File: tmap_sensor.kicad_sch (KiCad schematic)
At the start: 6 parts, among them J18 Conn_01x90_3Row_Socket, K2 1500A, K3 1502, K4 1500B, M2 Fan1, M3 Fan2

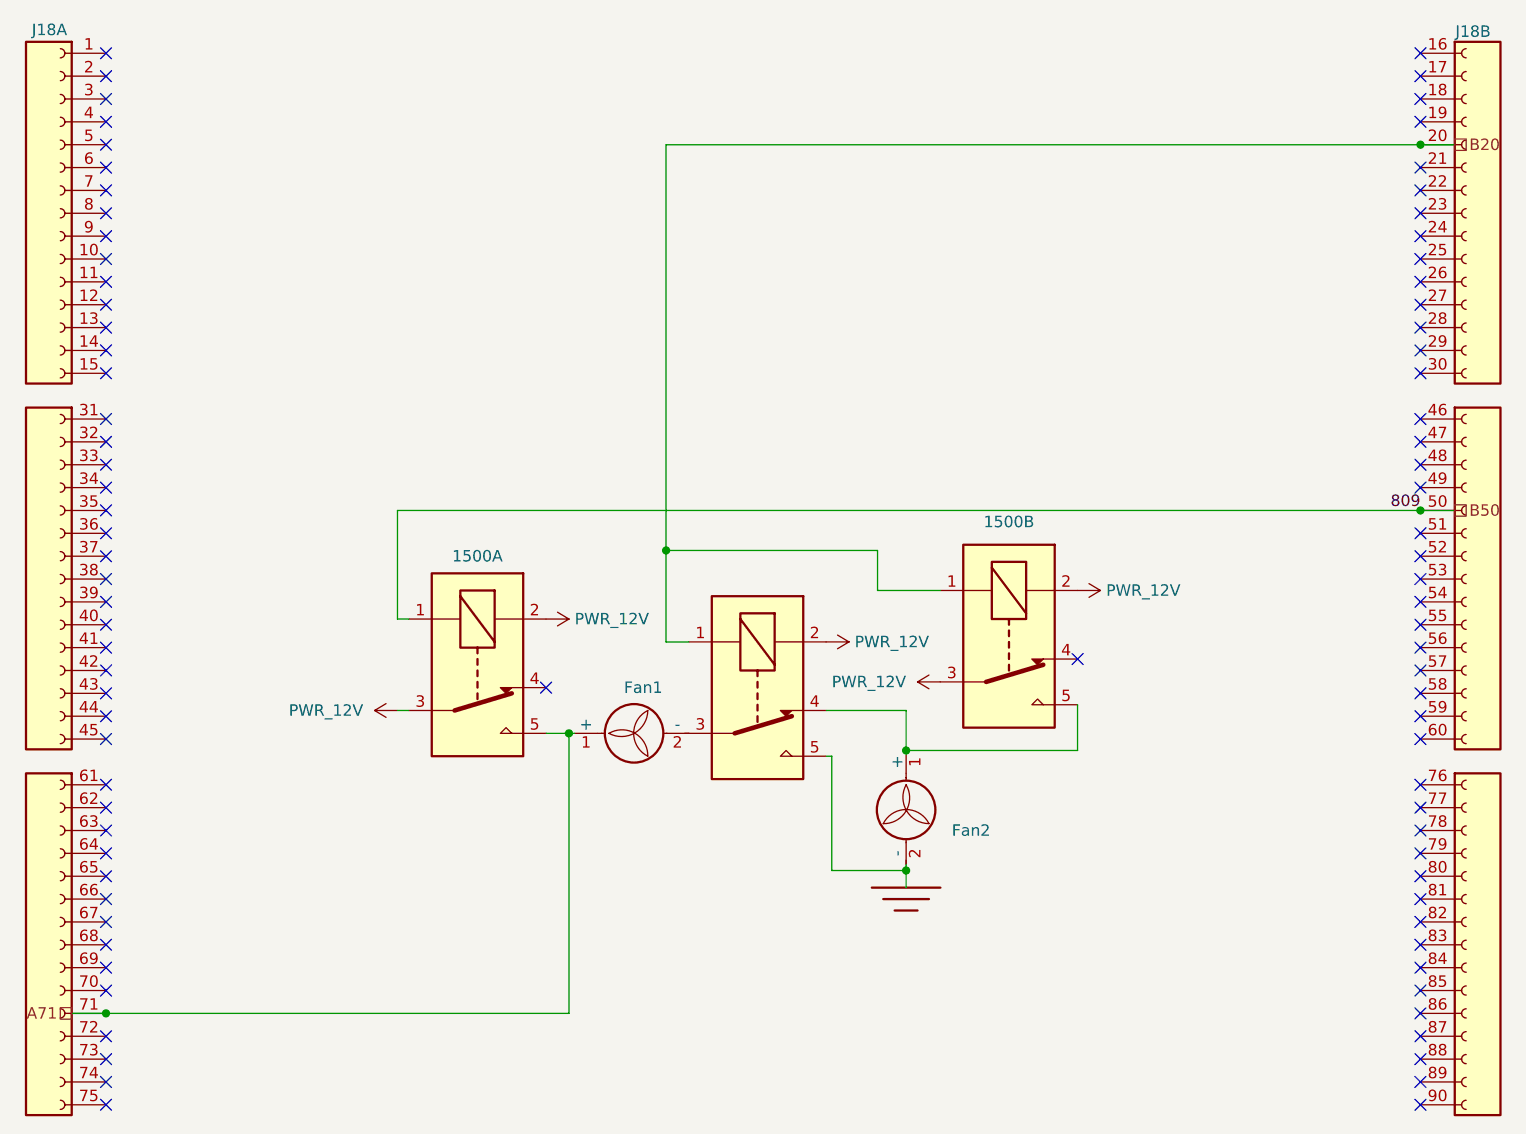
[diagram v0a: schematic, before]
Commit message: air conditioner updated
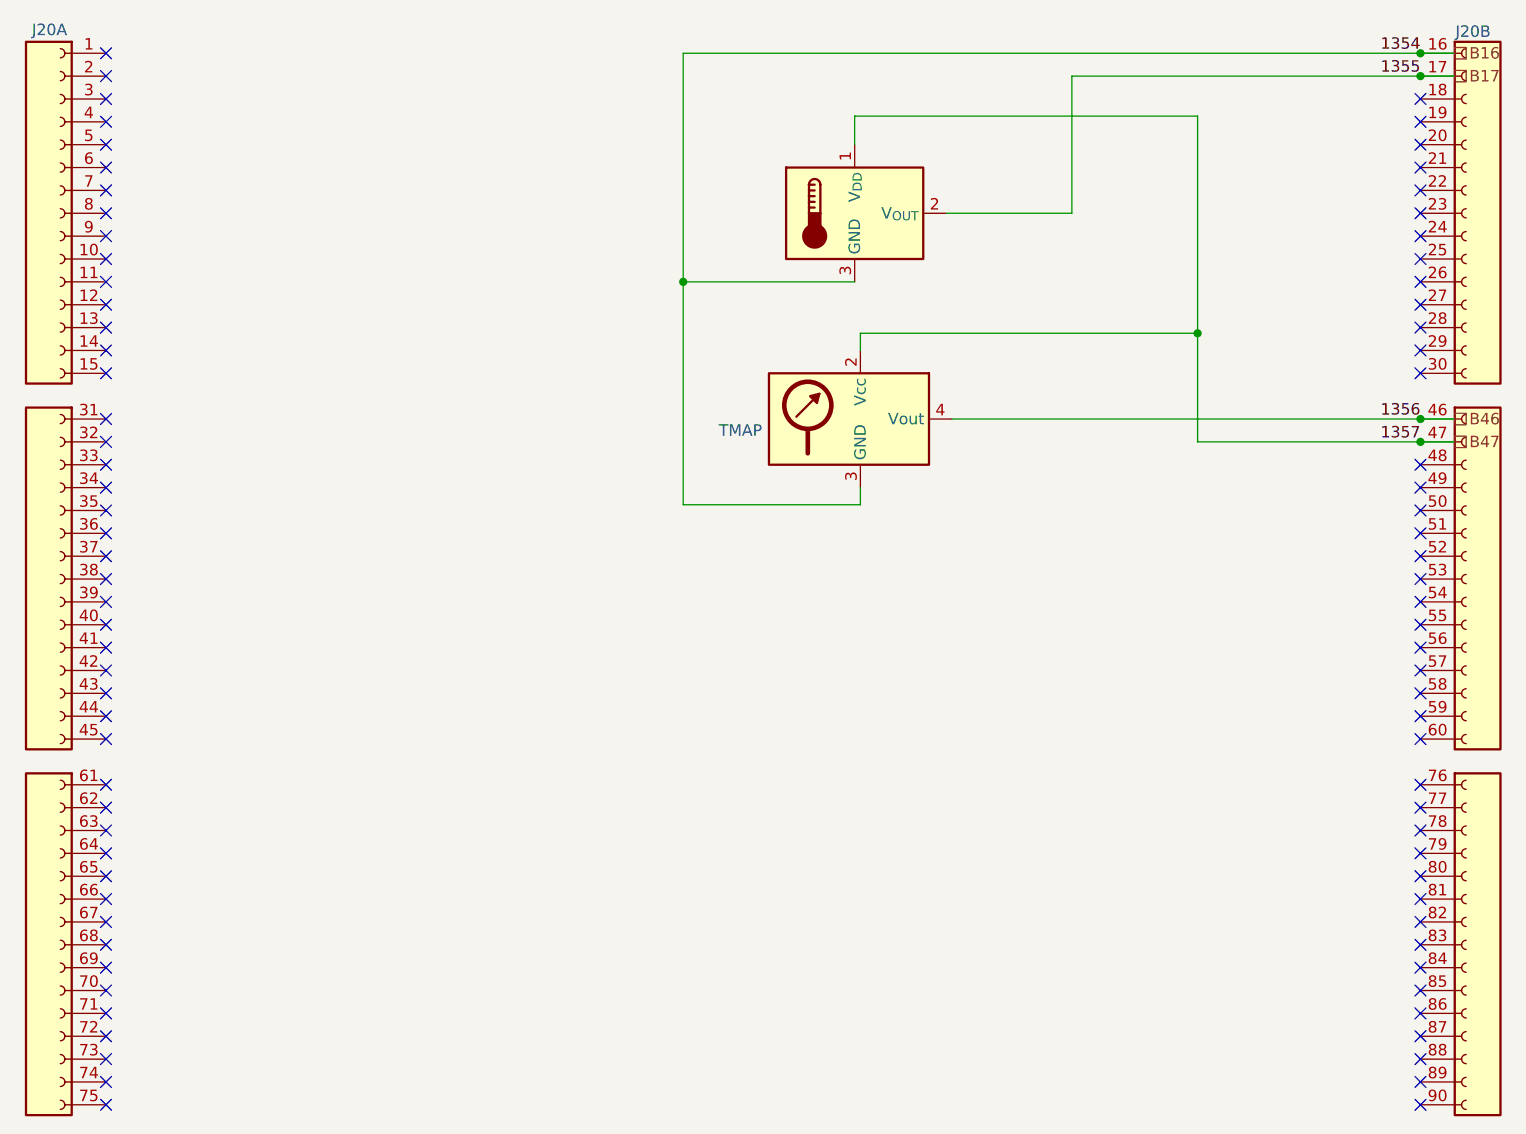
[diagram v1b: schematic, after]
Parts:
- removed J18: Conn_01x90_3Row_Socket, symbol sicma_socket:Conn_01x90_3Row_Socket
- removed K2: 1500A, PCM_SparkFun-Electromechanical:Relay_SPDT_20A_27.6x32.0mm, symbol SparkFun-Electromechanical:Relay_SPDT_20A_5V_27.6x32.0mm
- removed K3: 1502, PCM_SparkFun-Electromechanical:Relay_SPDT_20A_27.6x32.0mm, symbol SparkFun-Electromechanical:Relay_SPDT_20A_5V_27.6x32.0mm
- removed K4: 1500B, PCM_SparkFun-Electromechanical:Relay_SPDT_20A_27.6x32.0mm, symbol SparkFun-Electromechanical:Relay_SPDT_20A_5V_27.6x32.0mm
- removed M2: Fan1, symbol Motor:Fan
- removed M3: Fan2, symbol Motor:Fan
- added J20: Conn_01x90_3Row_Socket, symbol sicma_socket:Conn_01x90_3Row_Socket
- added U51: MCP9700Ax-ETT, Package_TO_SOT_SMD:SOT-23, symbol Sensor_Temperature:MCP9700Ax-ETT
- added U52: TMAP, symbol Sensor_Pressure:MPXHZ6115A
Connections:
- new net B16: J20.16 (B16), U51.3 (GND), U52.3 (GND)
- new net B17: J20.17 (B17), U51.2 (V_{OUT})
- new net B46: J20.46 (B46), U52.4 (Vout)
- new net B47: J20.47 (B47), U51.1 (V_{DD}), U52.2 (Vcc)
- no-connect marks 89 -> 86
